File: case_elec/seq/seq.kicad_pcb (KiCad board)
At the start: 2 copper layers, 71.1 x 79 mm, 15 parts, among them J1 LiPo, J10 Coupleur, J11 Jack, J2 B-, J3 BM, J4 B+, J5 P+, J6 P-, J7 Servo, J8 LEDs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

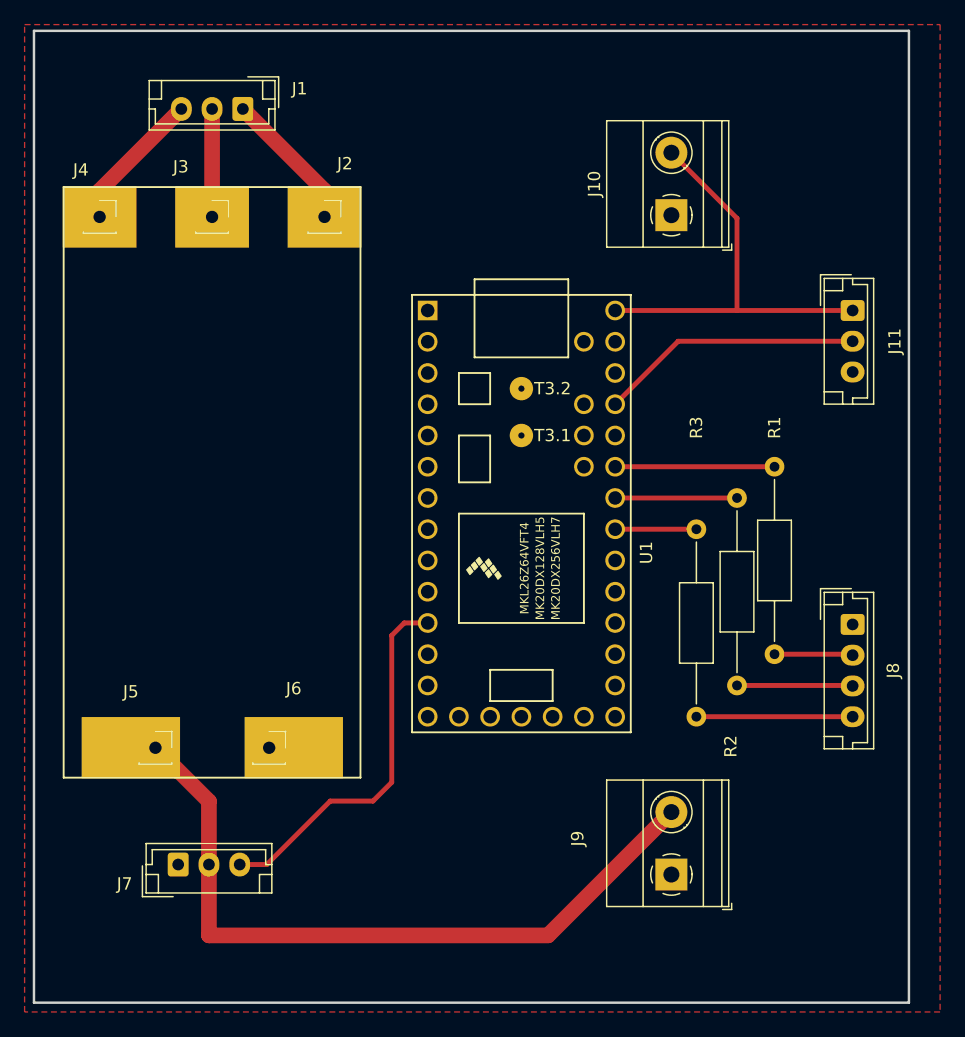
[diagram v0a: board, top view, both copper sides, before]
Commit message: sauvetage, màj seq version à usiner
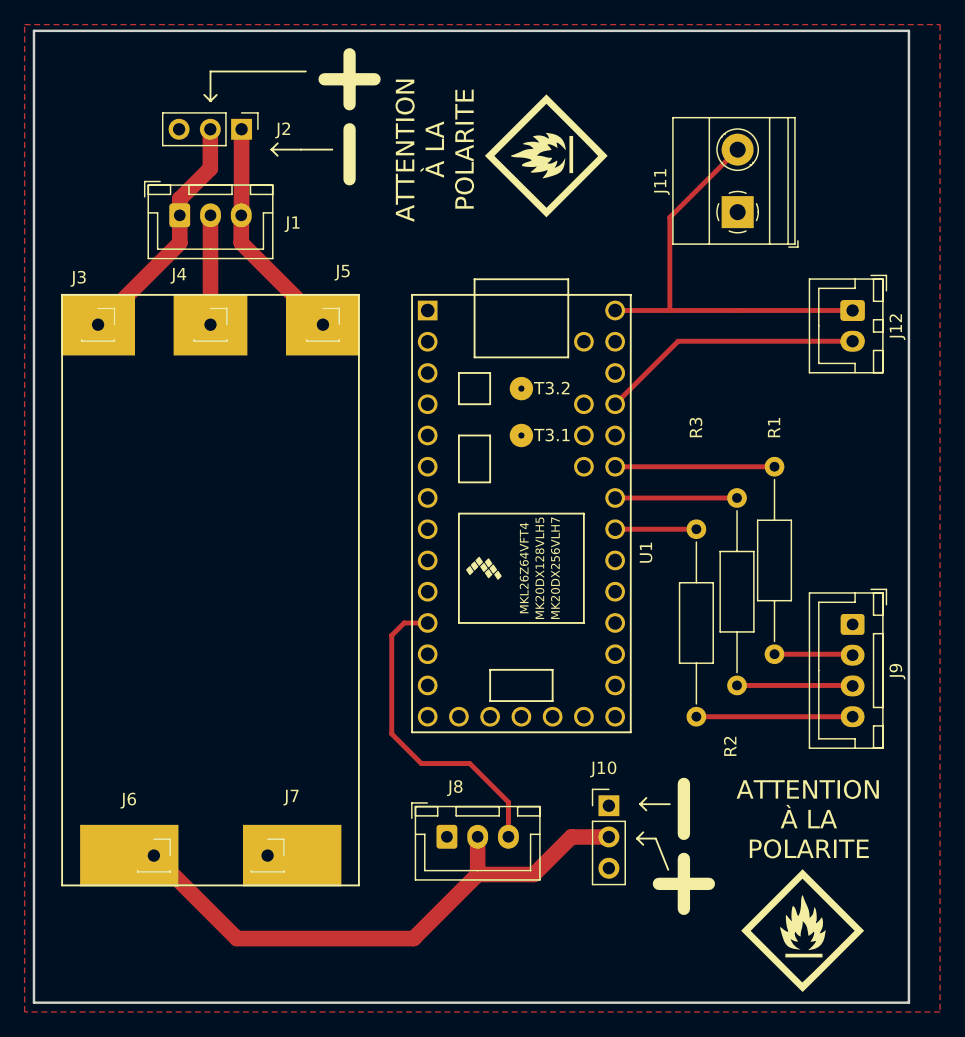
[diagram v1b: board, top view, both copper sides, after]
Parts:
- added G***: LOGO, LOGO, F.Cu at (128.0, 63.5)
- added G***: LOGO, LOGO, F.Cu at (148.8, 126.5)
- added J2: Lipo Alim, Connector_PinHeader_2.54mm:PinHeader_1x03_P2.54mm_Vertical, F.Cu at (103.2, 61.3)
- J1: value LiPo -> LiPo BMS; footprint Connector_JST:JST_EH_B3B-EH-A_1x03_P2.50mm_Vertical -> Connector_JST:JST_XH_B3B-XH-A_1x03_P2.50mm_Vertical
- J10: renamed from J9; footprint TerminalBlock_Phoenix:TerminalBlock_Phoenix_MKDS-1,5-2-5.08_1x02_P5.08mm_Horizontal -> Connector_PinHeader_2.54mm:PinHeader_1x03_P2.54mm_Vertical
- J12: renamed from J11; footprint Connector_JST:JST_EH_B3B-EH-A_1x03_P2.50mm_Vertical -> Connector_JST:JST_XH_B2B-XH-A_1x02_P2.50mm_Vertical
- J8: renamed from J7; footprint Connector_JST:JST_EH_B3B-EH-A_1x03_P2.50mm_Vertical -> Connector_JST:JST_XH_B3B-XH-A_1x03_P2.50mm_Vertical
- J9: renamed from J8; footprint Connector_JST:JST_EH_B4B-EH-A_1x04_P2.50mm_Vertical -> Connector_JST:JST_XH_B4B-XH-A_1x04_P2.50mm_Vertical
- moved J8 22.0 mm to (119.9, 118.9)
- moved J1 10.1 mm to (98.2, 68.3), turned to 0 degrees
- moved J6 8.76 mm to (96.1, 120.4)
- moved J7 8.76 mm to (105.4, 120.4)
- moved J3 8.76 mm to (91.6, 77.2)
- moved J4 8.76 mm to (100.7, 77.2)
- moved J5 8.76 mm to (109.9, 77.2)
- moved J10 7.56 mm to (133.1, 116.3), turned to 0 degrees
- moved J11 5.39 mm to (143.6, 68.1)
- renumbered J10 to J11, J4 to J3, J3 to J4, J2 to J5, J5 to J6, J6 to J7
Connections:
- net Net-(J1-Pad2) renamed /BM
- J1 pad 1: Net-(J1-Pad1) -> /B+
- J1 pad 3: Net-(J1-Pad3) -> /B-
- J3 pad 1: Net-(J1-Pad3) -> /B+
- J5 pad 1: Net-(J1-Pad1) -> /B-
- U1 pad 38: unconnected-(U1-Pad38) -> (no net)
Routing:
- net /B+: track 0.00 -> 19.7 mm
- net /B-: track 0.00 -> 18.6 mm
- net Net-(J10-Pad2): track 58.8 -> 46.3 mm
- net Net-(J1-Pad3): track 11.5 -> 0.00 mm
- net Net-(J1-Pad1): track 11.5 -> 0.00 mm
- net Net-(J8-Pad3): track 30.4 -> 25.9 mm
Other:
- board text added: "ATTENTION À LA POLARITE"
